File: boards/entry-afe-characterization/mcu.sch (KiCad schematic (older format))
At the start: 0 parts

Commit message: Continued work on AFE characterization board. Still have to do power supply.
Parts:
- added C26: 0.1 uF, symbol device:C
- added C6: 4.7 uF, symbol device:C
- added C7, C8: 0.47 uF, symbol device:C
- added J8: Conn_01x05, symbol Connector:Conn_01x05
- added J9: Conn_01x04, symbol Connector:Conn_01x04
- added R35: 10K, symbol device:R
- added U4: STM32F031G6U6TR, symbol st-azonenberg:STM32F031-QFN28
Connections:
- new net: R35.1, U4.1 (BOOT0)
- new net 3V3: C6.1, C7.1, C8.1, J8.1 (Pin_1), J9.1 (Pin_1), U4.17 (VDD), U4.5 (VDDA)
- new net DAC_CS_N: U4.9 (PA3)
- new net DAC_LDAC: U4.8 (PA2)
- new net DAC_RST_N: U4.13 (PA7)
- new net GAIN2_PWRUP: U4.10 (PA4)
- new net GAIN_PWRUP: U4.18 (PA8)
- new net GND: C26.2, C6.2, C7.2, C8.2, J8.2 (Pin_2), J9.4 (Pin_4), R35.2, U4.16 (VSS)
- new net INPUT_RST: U4.14 (PB0)
- new net OVERVOLTAGE_N: U4.27 (PB6)
- new net RELAY_EN: U4.15 (PB1)
- new net RST_N: C26.1, J8.5 (Pin_5), U4.4 (~RST)
- new net SPI_CS_A_N: U4.6 (PA0)
- new net SPI_CS_B_N: U4.7 (PA1)
- new net SPI_SCK: U4.24 (PB3)
- new net SPI_SDIO: U4.25 (PB4), U4.26 (PB5)
- new net SWCLK: J8.3 (Pin_3), U4.22 (PA14)
- new net SWDIO: J8.4 (Pin_4), U4.21 (PA13)
- new net UART_RX: J9.3 (Pin_3), U4.20 (PA10)
- new net UART_TX: J9.2 (Pin_2), U4.19 (PA9)
- new net VGA_PERF_MODE: U4.23 (PA15)
- no-connect marks 0 -> 5
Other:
- note added: "ADL5205 has 2.4V Vih\nso 3.3V inputs are OK\n\nSPI_SDIO and OVERVOLTAGE_N must be 5V tolerant"
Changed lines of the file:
@@
 $Descr A4 11693 8268
 encoding utf-8
-Sheet 4 8
+Sheet 3 8
 Title "Entry-Level Oscilloscope AFE Characterization Platform"
-Date "2020-03-17"
+Date "2020-03-24"
 Rev "0.1"
 Comp "Antikernel Labs"
@@
 Comment4 ""
 $EndDescr
+$Comp
+L st-azonenberg:STM32F031-QFN28 U4
+U 1 1 5E7D02B3
+P 3600 3850
+F 0 "U4" H 3600 3800 50  0000 L CNN
+F 1 "STM32F031G6U6TR" H 3600 3700 50  0000 L CNN
+F 2 "" H 3600 3850 50  0001 C CNN
+F 3 "" H 3600 3850 50  0001 C CNN
+	1    3600 3850
+	1    0    0    -1
+$EndComp
+$Comp
+L st-azonenberg:STM32F031-QFN28 U4
+U 2 1 5E7D1448
+P 5400 4350
+F 0 "U4" H 5400 4300 50  0000 L CNN
+F 1 "STM32F031G6U6TR" H 5400 4200 50  0000 L CNN
+F 2 "" H 5400 4350 50  0001 C CNN
+F 3 "" H 5400 4350 50  0001 C CNN
+	2    5400 4350
+	1    0    0    -1
+$EndComp
+$Comp
+L Connector:Conn_01x05 J8
+U 1 1 5E7D3D4D
+P 2250 2550
+F 0 "J8" H 2168 2967 50  0000 C CNN
+F 1 "Conn_01x05" H 2168 2876 50  0000 C CNN
+F 2 "" H 2250 2550 50  0001 C CNN
+F 3 "~" H 2250 2550 50  0001 C CNN
+	1    2250 2550
+	-1   0    0    -1
+$EndComp
+Text HLabel 2450 2350 2    50   Input ~ 0
+3V3
+Text HLabel 2450 2450 2    50   Input ~ 0
+GND
+Text Label 2700 2550 0    50   ~ 0
+SWCLK
+Wire Wire Line
+	2700 2550 2450 2550
+Text Label 2700 2650 0    50   ~ 0
+SWDIO
+Wire Wire Line
+	2700 2650 2450 2650
+Text Label 2700 2750 0    50   ~ 0
+RST_N
+Wire Wire Line
+	2700 2750 2450 2750
+Text Label 3500 3000 2    50   ~ 0
+3V3
+Text Label 3500 3100 2    50   ~ 0
+3V3
+Text Label 3500 3200 2    50   ~ 0
+GND
+$Comp
+L device:C C6
+U 1 1 5E7D8CE5
+P 3850 2400
+F 0 "C6" H 3965 2446 50  0000 L CNN
+F 1 "4.7 uF" H 3965 2355 50  0000 L CNN
+F 2 "" H 3888 2250 50  0001 C CNN
+F 3 "" H 3850 2400 50  0001 C CNN
+	1    3850 2400
+	1    0    0    -1
+$EndComp
+Text Label 3850 2250 2    50   ~ 0
+3V3
+Text Label 3850 2550 2    50   ~ 0
+GND
+$Comp
+L device:C C7
+U 1 1 5E7D94D8
+P 4350 2400
+F 0 "C7" H 4465 2446 50  0000 L CNN
+F 1 "0.47 uF" H 4465 2355 50  0000 L CNN
+F 2 "" H 4388 2250 50  0001 C CNN
+F 3 "" H 4350 2400 50  0001 C CNN
+	1    4350 2400
+	1    0    0    -1
+$EndComp
+$Comp
+L device:C C8
+U 1 1 5E7D977E
+P 4900 2400
+F 0 "C8" H 5015 2446 50  0000 L CNN
+F 1 "0.47 uF" H 5015 2355 50  0000 L CNN
+F 2 "" H 4938 2250 50  0001 C CNN
+F 3 "" H 4900 2400 50  0001 C CNN
+	1    4900 2400
+	1    0    0    -1
+$EndComp
+Wire Wire Line
+	4900 2250 4350 2250
+Connection ~ 4350 2250
+Wire Wire Line
+	4350 2250 3850 2250
+Wire Wire Line
+	3850 2550 4350 2550
+Connection ~ 4350 2550
+Wire Wire Line
+	4350 2550 4900 2550
+Text Label 3500 3400 2    50   ~ 0
+RST_N
+Text Label 2350 3050 2    50   ~ 0
+GND
+Wire Wire Line
+	2350 3050 2450 3050
+$Comp
+L device:R R35
+U 1 1 5E7DB482
+P 3200 3500
+F 0 "R35" V 3150 3350 50  0000 C CNN
+F 1 "10K" V 3200 3500 50  0000 C CNN
+F 2 "" V 3130 3500 50  0001 C CNN
+F 3 "" H 3200 3500 50  0001 C CNN
+	1    3200 3500
+	0    1    1    0
+$EndComp
+Wire Wire Line
+	3350 3500 3500 3500
+Text Label 2900 3500 2    50   ~ 0
+GND
+Wire Wire Line
+	2900 3500 3050 3500
+Text HLabel 5300 3800 0    50   Output ~ 0
+GAIN_PWRUP
+Text HLabel 5300 3400 0    50   Output ~ 0
+GAIN2_PWRUP
+Text Notes 5400 4950 0    50   ~ 0
+ADL5205 has 2.4V Vih\nso 3.3V inputs are OK\n\nSPI_SDIO and OVERVOLTAGE_N must be 5V tolerant
+Text HLabel 5300 4300 0    50   Output ~ 0
+VGA_PERF_MODE
+Text HLabel 5300 3000 0    50   Output ~ 0
+SPI_CS_A_N
+Text HLabel 5300 3100 0    50   Output ~ 0
+SPI_CS_B_N
+Text HLabel 6850 3200 0    50   Output ~ 0
+SPI_SCK
+Text HLabel 6850 3300 0    50   BiDi ~ 0
+SPI_SDIO
+Text Label 5300 4100 2    50   ~ 0
+SWDIO
+Text Label 5300 4200 2    50   ~ 0
+SWCLK
+$Comp
+L Connector:Conn_01x04 J9
+U 1 1 5E7DF065
+P 2250 4150
+F 0 "J9" H 2168 4467 50  0000 C CNN
+F 1 "Conn_01x04" H 2168 4376 50  0000 C CNN
+F 2 "" H 2250 4150 50  0001 C CNN
+F 3 "~" H 2250 4150 50  0001 C CNN
+	1    2250 4150
+	-1   0    0    -1
+$EndComp
+Text Label 2450 4050 0    50   ~ 0
+3V3
+Text Label 2450 4150 0    50   ~ 0
+UART_TX
+Text Label 2450 4250 0    50   ~ 0
+UART_RX
+Text Label 2450 4350 0    50   ~ 0
+GND
+Text Label 5300 3900 2    50   ~ 0
+UART_TX
+Text Label 5300 4000 2    50   ~ 0
+UART_RX
+NoConn ~ 5300 3600
+NoConn ~ 5300 3500
+Wire Wire Line
+	6850 3300 6850 3400
+NoConn ~ 6850 3600
+NoConn ~ 3500 3700
+NoConn ~ 3500 3800
+Text HLabel 5300 3300 0    50   Output ~ 0
+DAC_CS_N
+Text HLabel 5300 3200 0    50   Output ~ 0
+DAC_LDAC
+Text HLabel 5300 3700 0    50   Output ~ 0
+DAC_RST_N
+$Comp
+L device:C C26
+U 1 1 5E7F7A1A
+P 2450 2900
+F 0 "C26" H 2565 2946 50  0000 L CNN
+F 1 "0.1 uF" H 2565 2855 50  0000 L CNN
+F 2 "" H 2488 2750 50  0001 C CNN
+F 3 "" H 2450 2900 50  0001 C CNN
+	1    2450 2900
+	1    0    0    -1
+$EndComp
+Connection ~ 2450 2750
+Text HLabel 6850 3100 0    50   Output ~ 0
+RELAY_EN
+Text HLabel 6850 3500 0    50   Input ~ 0
+OVERVOLTAGE_N
+Text HLabel 6850 3000 0    50   Output ~ 0
+INPUT_RST
+$Comp
+L st-azonenberg:STM32F031-QFN28 U4
+U 3 1 5E7D219F
+P 6950 3650
+F 0 "U4" H 6950 3600 50  0000 L CNN
+F 1 "STM32F031G6U6TR" H 6950 3500 50  0000 L CNN
+F 2 "" H 6950 3650 50  0001 C CNN
+F 3 "" H 6950 3650 50  0001 C CNN
+	3    6950 3650
+	1    0    0    -1
+$EndComp
 $EndSCHEMATC

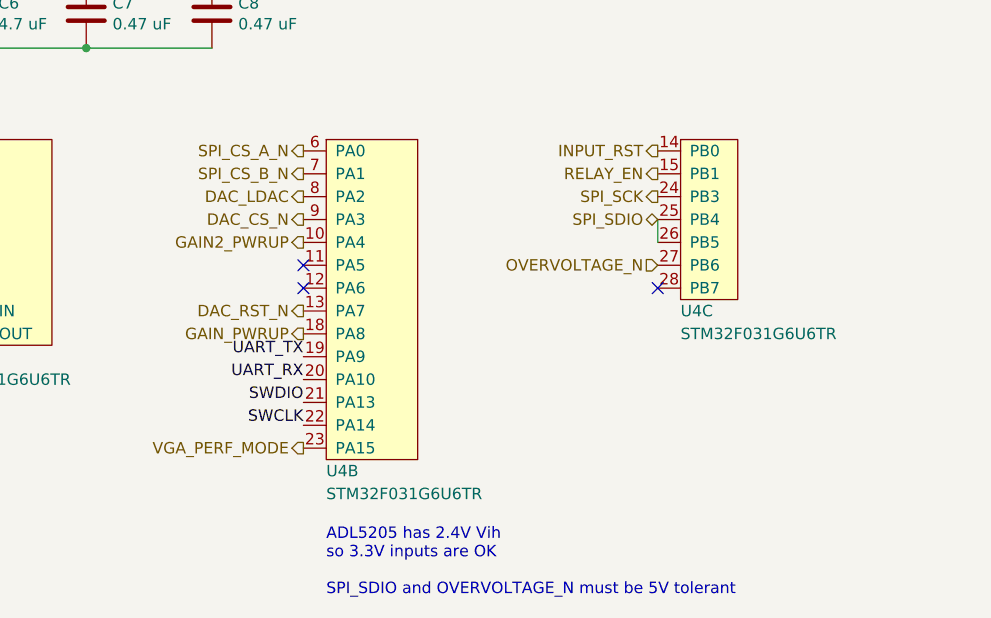
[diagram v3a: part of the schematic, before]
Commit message: Continued design review, added U18 to offset stage
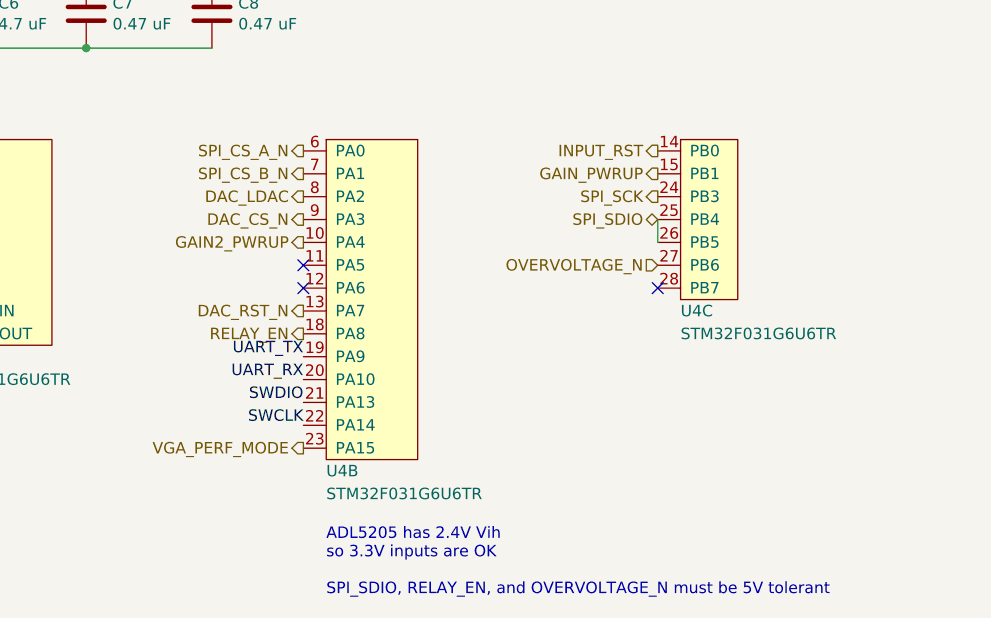
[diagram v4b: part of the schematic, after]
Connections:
- net GAIN_PWRUP: now also U4.15 (PB1); no longer U4.18 (PA8)
- net RELAY_EN: now also U4.18 (PA8); no longer U4.15 (PB1)
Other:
- note added: "ADL5205 has 2.4V Vih\nso 3.3V inputs are OK\n\nSPI_SDIO, RELAY_EN, and OVERVOLTAGE_N must be 5V tolerant"
- note removed: "ADL5205 has 2.4V Vih\nso 3.3V inputs are OK\n\nSPI_SDIO and OVERVOLTAGE_N must be 5V tolerant"
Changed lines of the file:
@@
 $Descr A4 11693 8268
 encoding utf-8
-Sheet 3 8
+Sheet 2 8
 Title "Entry-Level Oscilloscope AFE Characterization Platform"
-Date "2020-03-26"
+Date "2020-03-27"
 Rev "0.1"
 Comp "Antikernel Labs"
@@
 Wire Wire Line
 	2900 3500 3050 3500
-Text HLabel 5300 3800 0    50   Output ~ 0
+Text HLabel 6850 3100 0    50   Output ~ 0
 GAIN_PWRUP
 Text HLabel 5300 3400 0    50   Output ~ 0
 GAIN2_PWRUP
 Text Notes 5400 4950 0    50   ~ 0
-ADL5205 has 2.4V Vih\nso 3.3V inputs are OK\n\nSPI_SDIO and OVERVOLTAGE_N must be 5V tolerant
+ADL5205 has 2.4V Vih\nso 3.3V inputs are OK\n\nSPI_SDIO, RELAY_EN, and OVERVOLTAGE_N must be 5V tolerant
 Text HLabel 5300 4300 0    50   Output ~ 0
 VGA_PERF_MODE
@@
 $EndComp
 Connection ~ 2450 2750
-Text HLabel 6850 3100 0    50   Output ~ 0
+Text HLabel 5300 3800 0    50   Output ~ 0
 RELAY_EN
 Text HLabel 6850 3500 0    50   Input ~ 0

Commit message: Continued design review, began assigning footprints to sch symbols
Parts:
- C26, C7, C8: footprint (none) -> azonenberg_pcb:EIA_0402_CAP_NOSILK
- C6: footprint (none) -> azonenberg_pcb:EIA_0603_CAP_NOSILK
- J8: footprint (none) -> azonenberg_pcb:CONN_HEADER_2.54MM_1x5
- J9: footprint (none) -> azonenberg_pcb:CONN_HEADER_2.54MM_1x4
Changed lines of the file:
@@
 F 0 "J8" H 2168 2967 50  0000 C CNN
 F 1 "Conn_01x05" H 2168 2876 50  0000 C CNN
-F 2 "" H 2250 2550 50  0001 C CNN
+F 2 "azonenberg_pcb:CONN_HEADER_2.54MM_1x5" H 2250 2550 50  0001 C CNN
 F 3 "~" H 2250 2550 50  0001 C CNN
 	1    2250 2550
@@
 F 0 "C6" H 3965 2446 50  0000 L CNN
 F 1 "4.7 uF" H 3965 2355 50  0000 L CNN
-F 2 "" H 3888 2250 50  0001 C CNN
+F 2 "azonenberg_pcb:EIA_0603_CAP_NOSILK" H 3888 2250 50  0001 C CNN
 F 3 "" H 3850 2400 50  0001 C CNN
 	1    3850 2400
@@
 F 0 "C7" H 4465 2446 50  0000 L CNN
 F 1 "0.47 uF" H 4465 2355 50  0000 L CNN
-F 2 "" H 4388 2250 50  0001 C CNN
+F 2 "azonenberg_pcb:EIA_0402_CAP_NOSILK" H 4388 2250 50  0001 C CNN
 F 3 "" H 4350 2400 50  0001 C CNN
 	1    4350 2400
@@
 F 0 "C8" H 5015 2446 50  0000 L CNN
 F 1 "0.47 uF" H 5015 2355 50  0000 L CNN
-F 2 "" H 4938 2250 50  0001 C CNN
+F 2 "azonenberg_pcb:EIA_0402_CAP_NOSILK" H 4938 2250 50  0001 C CNN
 F 3 "" H 4900 2400 50  0001 C CNN
 	1    4900 2400
@@
 F 0 "J9" H 2168 4467 50  0000 C CNN
 F 1 "Conn_01x04" H 2168 4376 50  0000 C CNN
-F 2 "" H 2250 4150 50  0001 C CNN
+F 2 "azonenberg_pcb:CONN_HEADER_2.54MM_1x4" H 2250 4150 50  0001 C CNN
 F 3 "~" H 2250 4150 50  0001 C CNN
 	1    2250 4150
@@
 F 0 "C26" H 2565 2946 50  0000 L CNN
 F 1 "0.1 uF" H 2565 2855 50  0000 L CNN
-F 2 "" H 2488 2750 50  0001 C CNN
+F 2 "azonenberg_pcb:EIA_0402_CAP_NOSILK" H 2488 2750 50  0001 C CNN
 F 3 "" H 2450 2900 50  0001 C CNN
 	1    2450 2900

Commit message: Continued assigning footprints
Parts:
- R35: footprint (none) -> azonenberg_pcb:EIA_0402_RES_NOSILK
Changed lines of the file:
@@
 F 0 "R35" V 3150 3350 50  0000 C CNN
 F 1 "10K" V 3200 3500 50  0000 C CNN
-F 2 "" V 3130 3500 50  0001 C CNN
+F 2 "azonenberg_pcb:EIA_0402_RES_NOSILK" V 3130 3500 50  0001 C CNN
 F 3 "" H 3200 3500 50  0001 C CNN
 	1    3200 3500

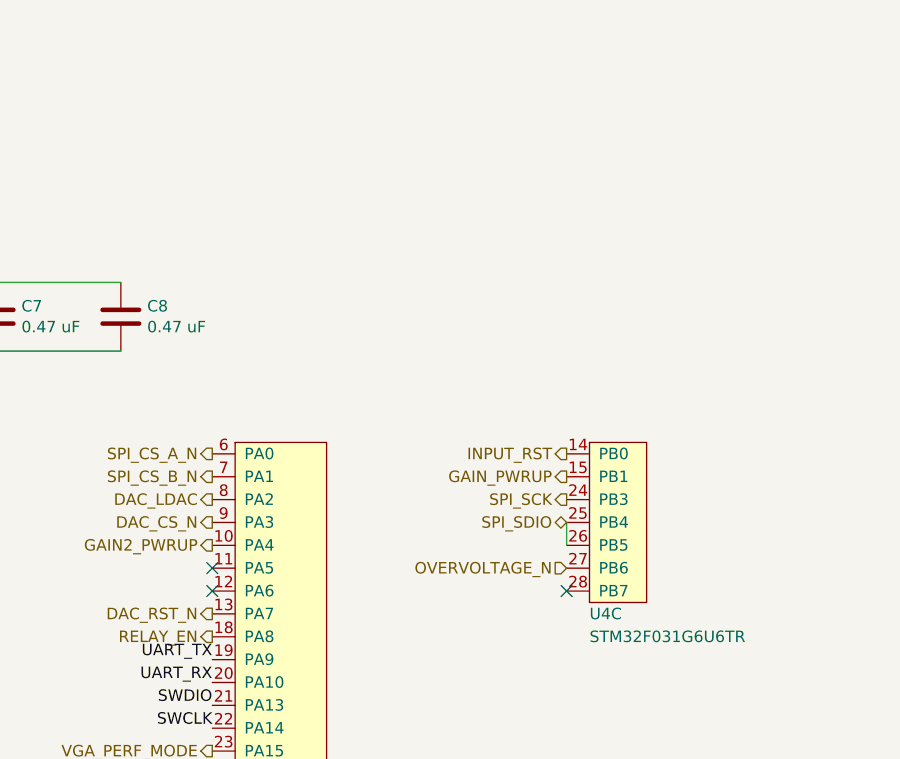
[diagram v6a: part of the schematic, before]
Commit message: Continued schematic review. Done with everything but test point/ground insertion.
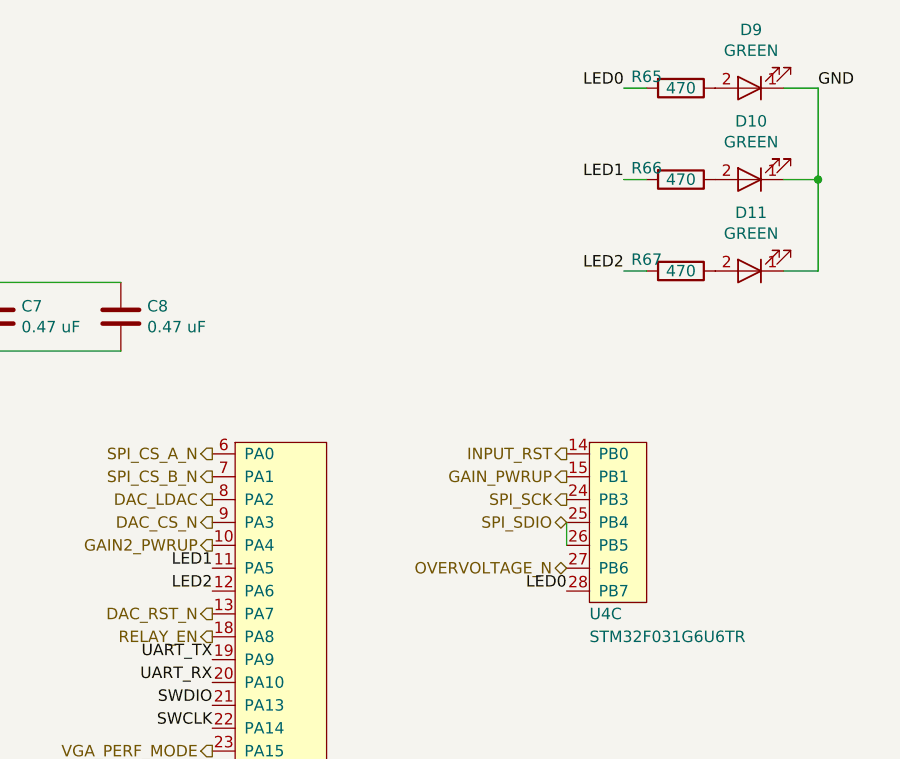
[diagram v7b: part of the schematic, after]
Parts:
- added D10, D11, D9: GREEN, azonenberg_pcb:EIA_0603_LED, symbol device:LED
- added R65, R66, R67: 470, azonenberg_pcb:EIA_0402_RES_NOSILK, symbol device:R
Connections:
- net GND: now also D10.1 (K), D11.1 (K), D9.1 (K)
- net LED1: now reaches U4.11 (PA5)
- net LED1: now also R66.2
- net LED2: now reaches U4.12 (PA6)
- net LED2: now also R67.2
- net LED0: now reaches U4.28 (PB7)
- net LED0: now also R65.2
- new net: D9.2 (A), R65.1
- new net: D10.2 (A), R66.1
- new net: D11.2 (A), R67.1
- no-connect marks 5 -> 2
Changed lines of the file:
@@
 Sheet 2 8
 Title "Entry-Level Oscilloscope AFE Characterization Platform"
-Date "2020-03-27"
+Date "2020-03-28"
 Rev "0.1"
 Comp "Antikernel Labs"
@@
 Text Label 5300 4000 2    50   ~ 0
 UART_RX
-NoConn ~ 5300 3600
-NoConn ~ 5300 3500
 Wire Wire Line
 	6850 3300 6850 3400
-NoConn ~ 6850 3600
 NoConn ~ 3500 3700
 NoConn ~ 3500 3800
@@
 Text HLabel 5300 3800 0    50   Output ~ 0
 RELAY_EN
-Text HLabel 6850 3500 0    50   Input ~ 0
+Text HLabel 6850 3500 0    50   BiDi ~ 0
 OVERVOLTAGE_N
 Text HLabel 6850 3000 0    50   Output ~ 0
@@
 	1    0    0    -1
 $EndComp
+Text Label 6850 3600 2    50   ~ 0
+LED0
+Text Label 7100 1400 2    50   ~ 0
+LED0
+Text Label 5300 3500 2    50   ~ 0
+LED1
+Text Label 5300 3600 2    50   ~ 0
+LED2
+$Comp
+L device:R R65
+U 1 1 5EAAECD4
+P 7350 1400
+F 0 "R65" V 7300 1250 50  0000 C CNN
+F 1 "470" V 7350 1400 50  0000 C CNN
+F 2 "azonenberg_pcb:EIA_0402_RES_NOSILK" V 7280 1400 50  0001 C CNN
+F 3 "" H 7350 1400 50  0001 C CNN
+	1    7350 1400
+	0    1    1    0
+$EndComp
+Wire Wire Line
+	7100 1400 7200 1400
+$Comp
+L device:LED D9
+U 1 1 5EAAF8A7
+P 7650 1400
+F 0 "D9" H 7643 1145 50  0000 C CNN
+F 1 "GREEN" H 7643 1236 50  0000 C CNN
+F 2 "azonenberg_pcb:EIA_0603_LED" H 7650 1400 50  0001 C CNN
+F 3 "~" H 7650 1400 50  0001 C CNN
+	1    7650 1400
+	-1   0    0    1
+$EndComp
+Text Label 7950 1400 0    50   ~ 0
+GND
+Wire Wire Line
+	7950 1400 7800 1400
+Text Label 7100 1800 2    50   ~ 0
+LED1
+$Comp
+L device:R R66
+U 1 1 5EAB0A48
+P 7350 1800
+F 0 "R66" V 7300 1650 50  0000 C CNN
+F 1 "470" V 7350 1800 50  0000 C CNN
+F 2 "azonenberg_pcb:EIA_0402_RES_NOSILK" V 7280 1800 50  0001 C CNN
+F 3 "" H 7350 1800 50  0001 C CNN
+	1    7350 1800
+	0    1    1    0
+$EndComp
+Wire Wire Line
+	7100 1800 7200 1800
+$Comp
+L device:LED D10
+U 1 1 5EAB0A53
+P 7650 1800
+F 0 "D10" H 7643 1545 50  0000 C CNN
+F 1 "GREEN" H 7643 1636 50  0000 C CNN
+F 2 "azonenberg_pcb:EIA_0603_LED" H 7650 1800 50  0001 C CNN
+F 3 "~" H 7650 1800 50  0001 C CNN
+	1    7650 1800
+	-1   0    0    1
+$EndComp
+Wire Wire Line
+	7950 1800 7800 1800
+Text Label 7100 2200 2    50   ~ 0
+LED2
+$Comp
+L device:R R67
+U 1 1 5EAB1BC4
+P 7350 2200
+F 0 "R67" V 7300 2050 50  0000 C CNN
+F 1 "470" V 7350 2200 50  0000 C CNN
+F 2 "azonenberg_pcb:EIA_0402_RES_NOSILK" V 7280 2200 50  0001 C CNN
+F 3 "" H 7350 2200 50  0001 C CNN
+	1    7350 2200
+	0    1    1    0
+$EndComp
+Wire Wire Line
+	7100 2200 7200 2200
+$Comp
+L device:LED D11
+U 1 1 5EAB1BCF
+P 7650 2200
+F 0 "D11" H 7643 1945 50  0000 C CNN
+F 1 "GREEN" H 7643 2036 50  0000 C CNN
+F 2 "azonenberg_pcb:EIA_0603_LED" H 7650 2200 50  0001 C CNN
+F 3 "~" H 7650 2200 50  0001 C CNN
+	1    7650 2200
+	-1   0    0    1
+$EndComp
+Wire Wire Line
+	7950 2200 7800 2200
+Wire Wire Line
+	7950 1400 7950 1800
+Connection ~ 7950 1800
+Wire Wire Line
+	7950 1800 7950 2200
 $EndSCHEMATC

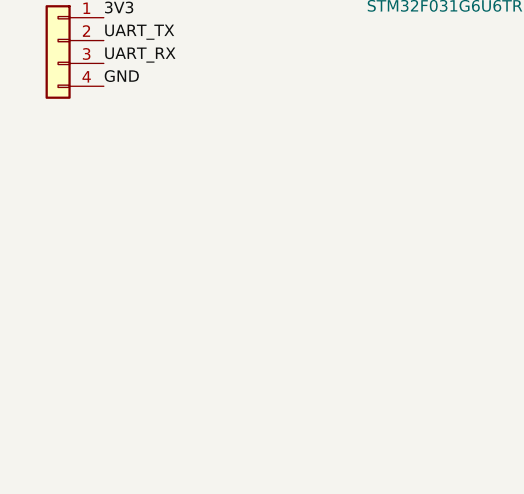
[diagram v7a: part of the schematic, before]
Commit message: Finished schematic review, assigned all footprints
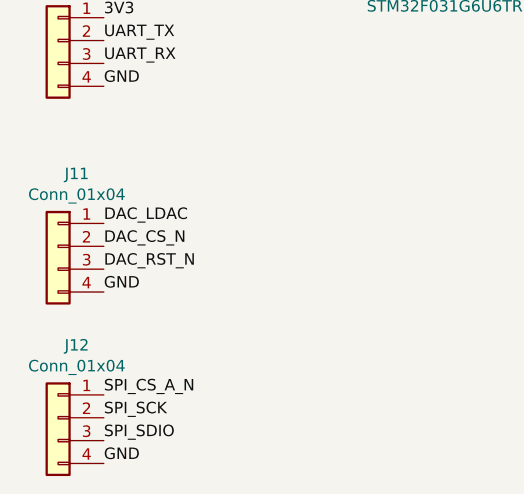
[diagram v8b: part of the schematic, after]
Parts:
- added J11, J12: Conn_01x04, azonenberg_pcb:CONN_HEADER_2.54MM_1x4, symbol Connector:Conn_01x04
- U4: footprint (none) -> azonenberg_pcb:QFN_28_0.5MM_4x4MM_NOPAD
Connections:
- net DAC_CS_N: now also J11.2 (Pin_2)
- net DAC_LDAC: now also J11.1 (Pin_1)
- net DAC_RST_N: now also J11.3 (Pin_3)
- net GND: now also J11.4 (Pin_4), J12.4 (Pin_4)
- net SPI_CS_A_N: now also J12.1 (Pin_1)
- net SPI_SCK: now also J12.2 (Pin_2)
- net SPI_SDIO: now also J12.3 (Pin_3)
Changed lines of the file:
@@
 F 0 "U4" H 3600 3800 50  0000 L CNN
 F 1 "STM32F031G6U6TR" H 3600 3700 50  0000 L CNN
-F 2 "" H 3600 3850 50  0001 C CNN
+F 2 "azonenberg_pcb:QFN_28_0.5MM_4x4MM_NOPAD" H 3600 3850 50  0001 C CNN
 F 3 "" H 3600 3850 50  0001 C CNN
 	1    3600 3850
@@
 F 0 "U4" H 5400 4300 50  0000 L CNN
 F 1 "STM32F031G6U6TR" H 5400 4200 50  0000 L CNN
-F 2 "" H 5400 4350 50  0001 C CNN
+F 2 "azonenberg_pcb:QFN_28_0.5MM_4x4MM_NOPAD" H 5400 4350 50  0001 C CNN
 F 3 "" H 5400 4350 50  0001 C CNN
 	2    5400 4350
@@
 F 0 "U4" H 6950 3600 50  0000 L CNN
 F 1 "STM32F031G6U6TR" H 6950 3500 50  0000 L CNN
-F 2 "" H 6950 3650 50  0001 C CNN
+F 2 "azonenberg_pcb:QFN_28_0.5MM_4x4MM_NOPAD" H 6950 3650 50  0001 C CNN
 F 3 "" H 6950 3650 50  0001 C CNN
 	3    6950 3650
@@
 Wire Wire Line
 	7950 1800 7950 2200
+Text Label 2450 5700 0    50   ~ 0
+SPI_CS_A_N
+Text Label 2450 4950 0    50   ~ 0
+DAC_LDAC
+Text Label 2450 5050 0    50   ~ 0
+DAC_CS_N
+Text Label 2450 5150 0    50   ~ 0
+DAC_RST_N
+$Comp
+L Connector:Conn_01x04 J11
+U 1 1 5EACF2C6
+P 2250 5050
+F 0 "J11" H 2168 5367 50  0000 C CNN
+F 1 "Conn_01x04" H 2168 5276 50  0000 C CNN
+F 2 "azonenberg_pcb:CONN_HEADER_2.54MM_1x4" H 2250 5050 50  0001 C CNN
+F 3 "~" H 2250 5050 50  0001 C CNN
+	1    2250 5050
+	-1   0    0    -1
+$EndComp
+$Comp
+L Connector:Conn_01x04 J12
+U 1 1 5EACF761
+P 2250 5800
+F 0 "J12" H 2168 6117 50  0000 C CNN
+F 1 "Conn_01x04" H 2168 6026 50  0000 C CNN
+F 2 "azonenberg_pcb:CONN_HEADER_2.54MM_1x4" H 2250 5800 50  0001 C CNN
+F 3 "~" H 2250 5800 50  0001 C CNN
+	1    2250 5800
+	-1   0    0    -1
+$EndComp
+Text Label 2450 5800 0    50   ~ 0
+SPI_SCK
+Text Label 2450 5900 0    50   ~ 0
+SPI_SDIO
+Text Label 2450 6000 0    50   ~ 0
+GND
+Text Label 2450 5250 0    50   ~ 0
+GND
 $EndSCHEMATC
